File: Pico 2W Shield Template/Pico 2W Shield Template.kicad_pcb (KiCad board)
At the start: 2 copper layers, 53.3 x 22.9 mm, 1 part

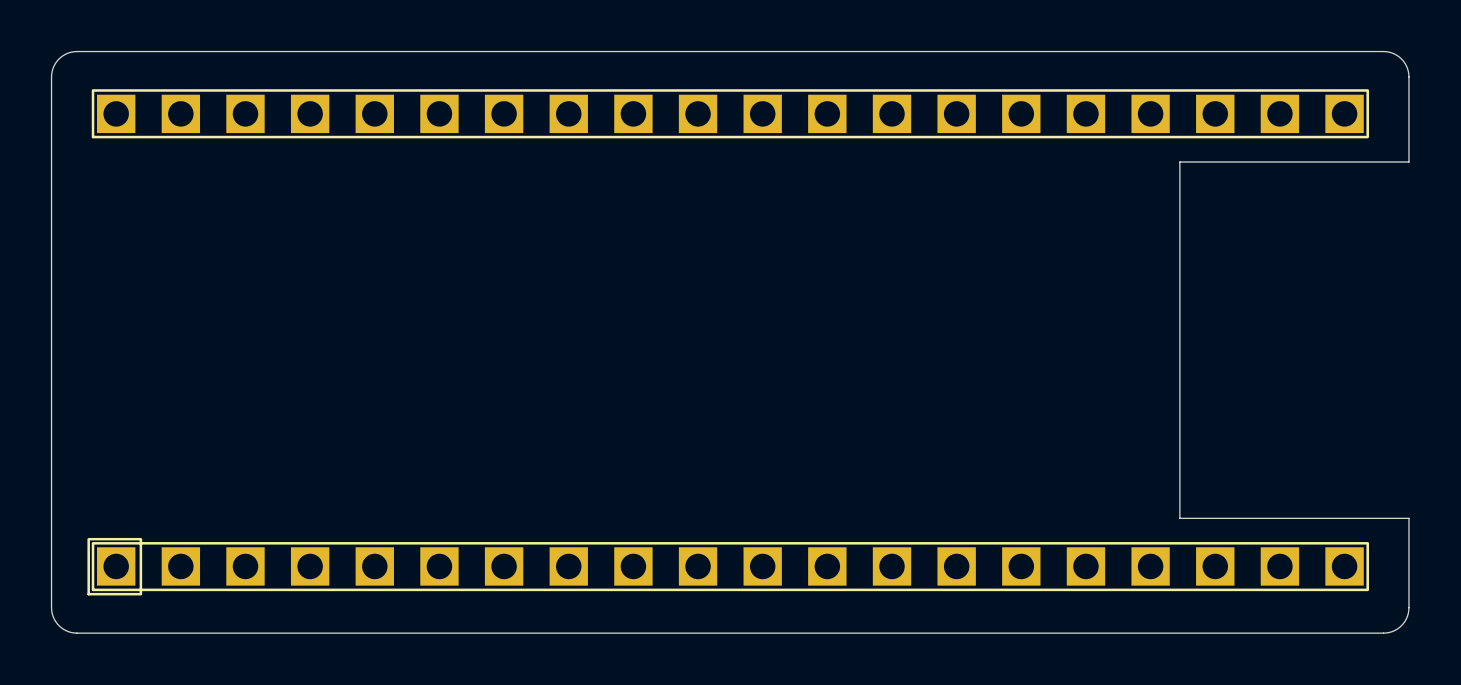
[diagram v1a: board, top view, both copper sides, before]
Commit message: Flip Pico shield assemblies and center USB reference markings
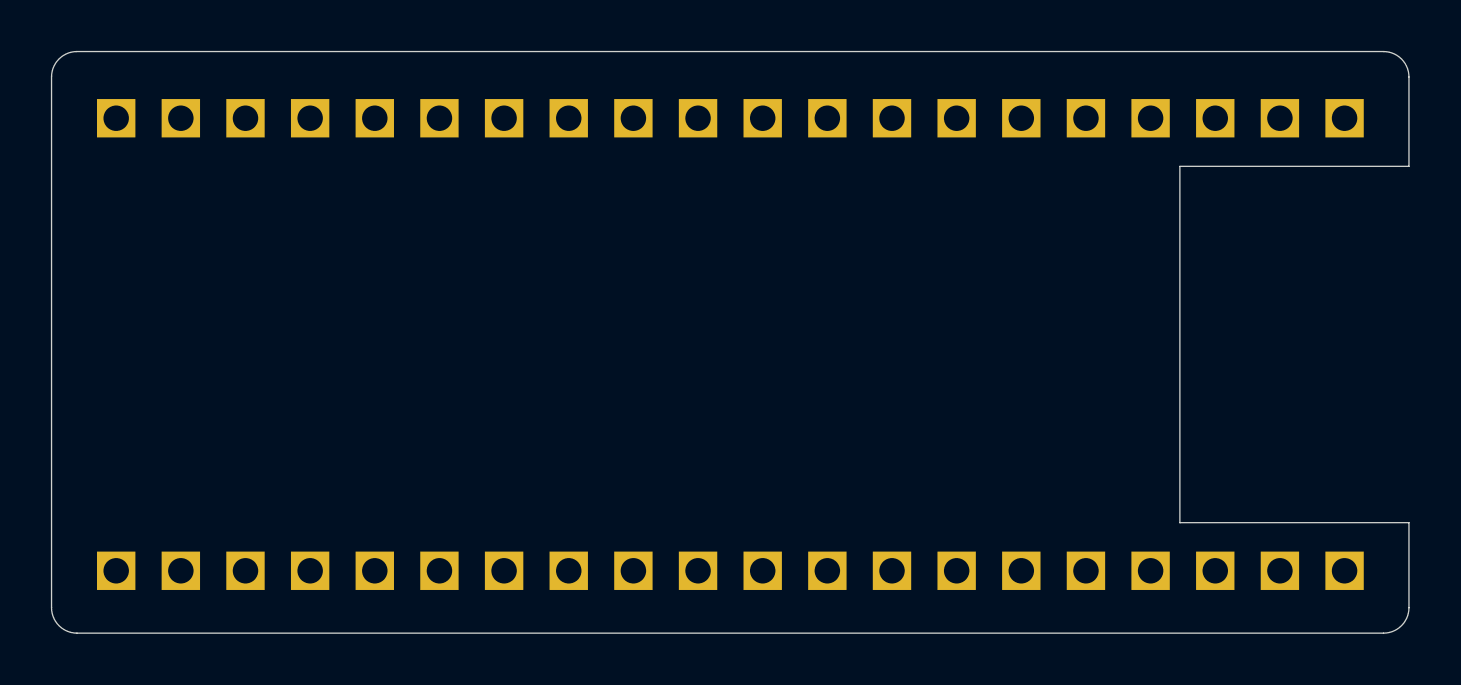
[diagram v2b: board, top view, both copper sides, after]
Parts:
- U1: moved to B.Cu
- moved U1 1.95 mm to (146.8, 90.8), turned to -90 degrees
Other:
- outline, holes or cut-outs redrawn
